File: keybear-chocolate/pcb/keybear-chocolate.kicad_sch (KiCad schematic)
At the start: 89 parts, among them J1 MJ-4PP-9, J2 OLED, J3 LED, P1 i2c-pin, P2 i2c-pin, SW1 SW_PUSH, SW10 SW_PUSH, SW11 SW_PUSH, SW12 SW_PUSH, SW13 SW_PUSH, SW14 SW_PUSH, SW15 SW_PUSH, SW16 SW_PUSH, SW17 SW_PUSH, SW18 SW_PUSH, SW19 SW_PUSH, SW2 SW_PUSH, SW20 SW_PUSH, SW21 SW_PUSH, SW25 Rotary_Encoder_Switch, SW3 SW_PUSH, SW4 SW_PUSH, SW5 SW_PUSH, SW6 SW_PUSH, SW7 SW_PUSH, SW8 SW_PUSH, SW9 SW_PUSH, U1 ProMicro

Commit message: updating keys
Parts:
- added D19, D23: D, kbd:D3_TH_SMD, symbol Device:D
- added L23: SK6812MINI, kbd:SK6812MINI_rev, symbol corne-chocolate-rescue:SK6812MINI-kbd
- added SW19, SW23: SW_PUSH, kbd:MX_ALPS_PG1350_noLed, symbol corne-chocolate-rescue:SW_PUSH-kbd
- L24: renamed from L23; footprint kbd:SK6812MINI_underglow -> kbd:SK6812MINI_rev
- L25: renamed from L24; footprint kbd:SK6812MINI_underglow -> kbd:SK6812MINI_rev
- L26: renamed from L25; footprint kbd:SK6812MINI_underglow -> kbd:SK6812MINI_rev
- L27: renamed from L26; footprint kbd:SK6812MINI_underglow -> kbd:SK6812MINI_rev
- L28: renamed from L27; footprint kbd:SK6812MINI_underglow -> kbd:SK6812MINI_rev
- L29: renamed from L28; footprint kbd:SK6812MINI_underglow -> kbd:SK6812MINI_rev
- SW1, SW2, SW3, SW4, SW5, SW6, SW7, SW8, SW9: footprint kbd:MX_ALPS_PG1350_noLed -> SofleChoc:Choc_Hotswap_SK6812MiniE
- renumbered D19 to D20, D20 to D21, D21 to D22, SW19 to SW20, SW20 to SW21, SW21 to SW22
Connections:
- net ENCA: now also U1.14 (B2)
- net ENCB: now also U1.13 (B6)
- net GND: now also L23.2 (VSS)
- net VCC: now also L23.4 (VDD)
- net col2: now also SW19.1
- net col3: now also SW23.1
- net row0: now also U1.8 (C6), D23.1 (K); no longer D1.1 (K), D2.1 (K), D3.1 (K), D4.1 (K), D5.1 (K), D6.1 (K), U1.7 (D4)
- net row1: now also D1.1 (K), D2.1 (K), D3.1 (K), D4.1 (K), D5.1 (K), D6.1 (K), U1.9 (D7); no longer D10.1 (K), D11.1 (K), D12.1 (K), D7.1 (K), D8.1 (K), D9.1 (K), U1.8 (C6)
- net row2: now also D10.1 (K), D11.1 (K), D12.1 (K), D7.1 (K), D8.1 (K), D9.1 (K), U1.10 (E6); no longer D13.1 (K), D14.1 (K), D15.1 (K), D16.1 (K), D17.1 (K), D18.1 (K), U1.9 (D7)
- net row3: now also D13.1 (K), D14.1 (K), D15.1 (K), D16.1 (K), D17.1 (K), D18.1 (K), U1.11 (B4); no longer D20.1 (K), D21.1 (K), D22.1 (K), U1.10 (E6)
- net row4: now reaches U1.12 (B5)
- net row4: now also D20.1 (K), D21.1 (K), D22.1 (K), D19.1 (K)
- net at L3.3 (DIN): now also L23.1 (DOUT); no longer L4.1 (DOUT)
- new net: L23.3 (DIN), L4.1 (DOUT)
- new net: D23.2 (A), SW23.2
- new net: D19.2 (A), SW19.2
- new net CS: U1.7 (D4)
- no-connect marks 6 -> 2
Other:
- moved on the sheet: D1, D10, D11, D12, D13, D14, D15, D16, D17, D18, D2, D20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

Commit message: updated latest kicad files
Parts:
- removed L23: SK6812MINI, kbd:SK6812MINI_rev, symbol corne-chocolate-rescue:SK6812MINI-kbd
- removed SW23: SW_PUSH, kbd:MX_ALPS_PG1350_noLed, symbol corne-chocolate-rescue:SW_PUSH-kbd
- added L19: SK6812MINI, kbd:SK6812MINI_rev, symbol corne-chocolate-rescue:SK6812MINI-kbd
- added SW19: SW_PUSH, kbd:Choc_Hotswap, symbol corne-chocolate-rescue:SW_PUSH-kbd
- D1, D10, D11, D12, D13, D14, D15, D16, D17, D18, D19, D20, D21, D22, D23, D3, D4, D5, D6, D7, D8, D9: footprint kbd:D3_TH_SMD -> kbd:D3_SMD
- D2: footprint kbd:D3_TH_SMD -> kbd:D3_SMD_v2
- SW10, SW11, SW12, SW13, SW14, SW15, SW16, SW17, SW18: footprint kbd:MX_ALPS_PG1350_noLed -> kbd:Choc_Hotswap
- SW20: renamed from SW19; footprint kbd:MX_ALPS_PG1350_noLed -> kbd:Choc_Hotswap
- SW21: renamed from SW20; footprint kbd:MX_ALPS_PG1350_noLed -> kbd:Choc_Hotswap
- SW22: renamed from SW21; footprint kbd:MX_ALPS_PG1350_noLed -> kbd:Choc_Hotswap
- SW23: renamed from SW22; footprint kbd:MX_ALPS_PG1350_noLed_1.75u -> kbd:Choc_Hotswap
- SW7, SW8, SW9: footprint SofleChoc:Choc_Hotswap_SK6812MiniE -> kbd:Choc_Hotswap
- renumbered L19 to L20, L20 to L21, L21 to L22, L22 to L23
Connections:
- net GND: now also L19.2 (VSS)
- net VCC: now also L19.4 (VDD)
- net col1: now also SW19.1
- net row0: now also D1.1 (K), D2.1 (K), D3.1 (K), D4.1 (K), D5.1 (K), D6.1 (K); no longer D23.1 (K)
- net row1: now also D10.1 (K), D11.1 (K), D12.1 (K), D7.1 (K), D8.1 (K), D9.1 (K); no longer D1.1 (K), D2.1 (K), D3.1 (K), D4.1 (K), D5.1 (K), D6.1 (K)
- net row2: now also D13.1 (K), D14.1 (K), D15.1 (K), D16.1 (K), D17.1 (K), D18.1 (K); no longer D10.1 (K), D11.1 (K), D12.1 (K), D7.1 (K), D8.1 (K), D9.1 (K)
- net row3: now also D19.1 (K), D20.1 (K), D21.1 (K), D22.1 (K), D23.1 (K); no longer D13.1 (K), D14.1 (K), D15.1 (K), D16.1 (K), D17.1 (K), D18.1 (K)
- net at L3.3 (DIN): now also L4.1 (DOUT)
- net at L14.3 (DIN): now also L19.1 (DOUT); no longer L20.1 (DOUT)
- net at D23.2 (A): now also SW19.2
- removed net row4: D19.1 (K), D20.1 (K), D21.1 (K), D22.1 (K), U1.12 (B5)
- new net: L19.3 (DIN), L20.1 (DOUT)
- no-connect marks 2 -> 3
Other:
- moved on the sheet: L24, L25, L26, L27, L28, L29, SW25, U1

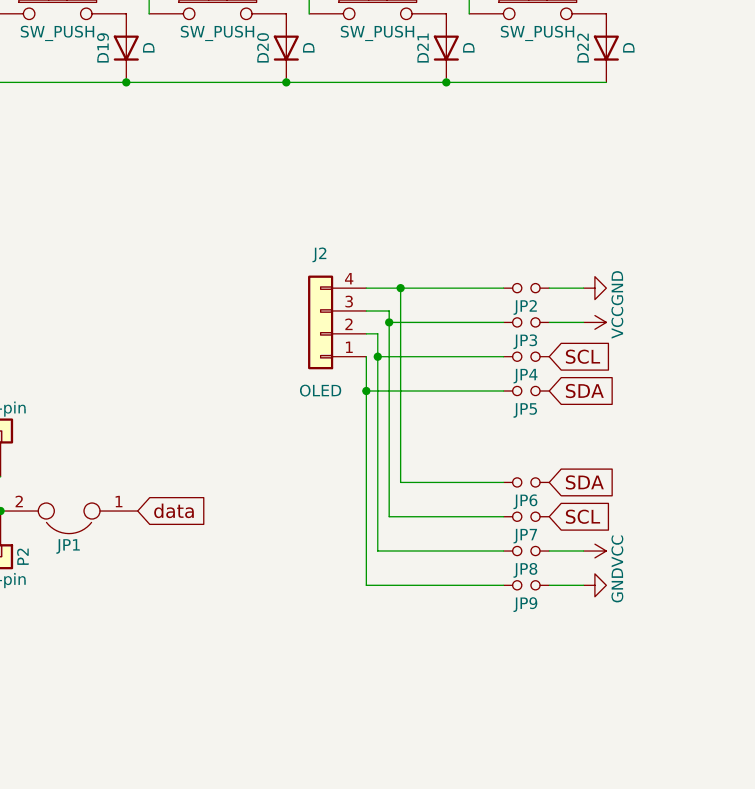
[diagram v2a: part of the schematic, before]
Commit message: OLED port updated to 5 pins
OLED port updated to 5 pins to support NiceView! out of the box
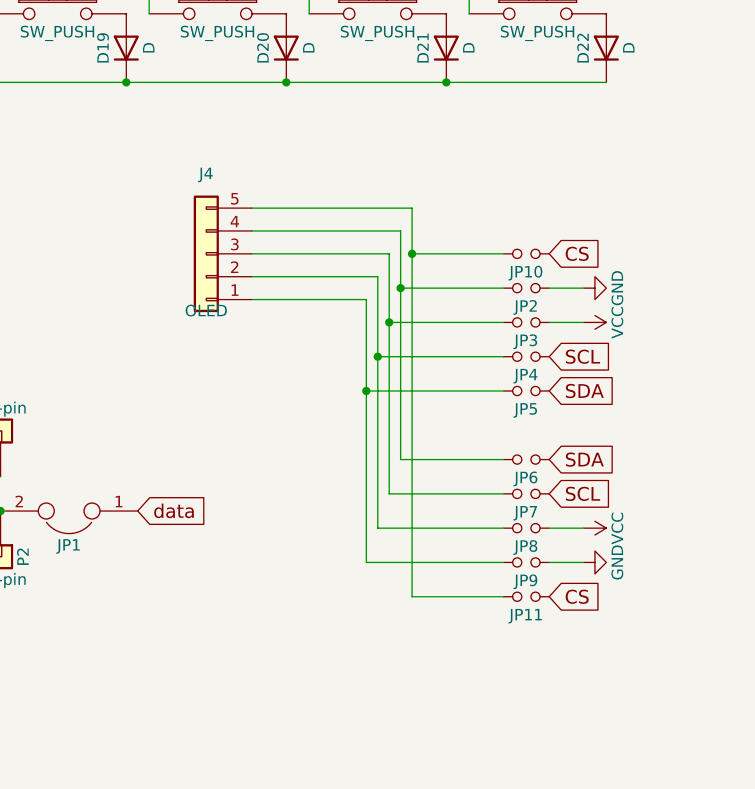
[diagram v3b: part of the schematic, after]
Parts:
- removed J2: OLED, kbd:OLED, symbol Connector_Generic:Conn_01x04
- added J4: OLED, kbd:OLED, symbol Connector_Generic:Conn_01x05
- added JP10, JP11: (no value), kbd:Jumper, symbol corne-chocolate-rescue:Jumper_NO_Small-Device
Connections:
- net CS: now also JP10.1, JP11.1
- net at JP5.2, JP9.2: now also J4.1 (Pin_1)
- net at JP4.2, JP8.2: now also J4.2 (Pin_2)
- net at JP3.2, JP7.2: now also J4.3 (Pin_3)
- net at JP2.2, JP6.2: now also J4.4 (Pin_4)
- new net: J4.5 (Pin_5), JP10.2, JP11.2
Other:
- moved on the sheet: JP6, JP7, JP8, JP9

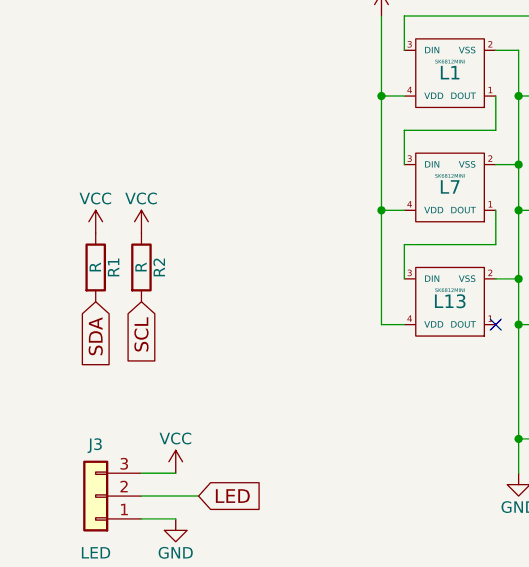
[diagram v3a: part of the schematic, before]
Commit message: OLED Resistence removed
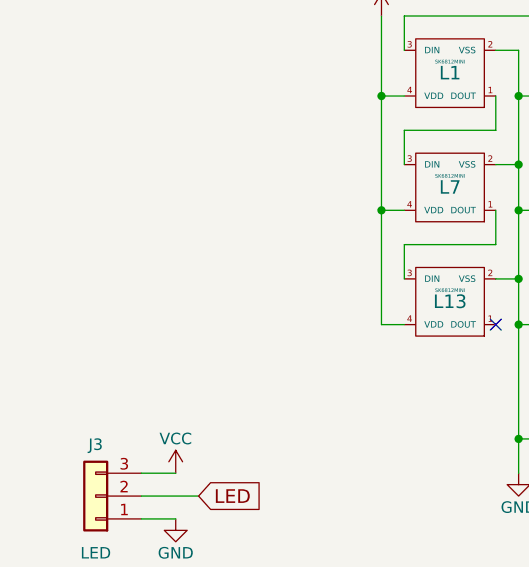
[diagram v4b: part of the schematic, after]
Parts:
- removed R1, R2: R, kbd:R, symbol Device:R
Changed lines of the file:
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@@
-    )
-  )
-  (global_label "SCL" (shape input) (at 30.48 163.83 270) (fields_autoplaced)
-    (effects (font (size 1.524 1.524)) (justify right))
-    (property "Intersheetrefs" "${INTERSHEET_REFS}" (at 30.48 170.8359 90)
-      (effects (font (size 1.27 1.27)) (justify right) hide)
     )
   )
@@
     (effects (font (size 1.1938 1.1938)) (justify right))
     (property "Intersheetrefs" "${INTERSHEET_REFS}" (at 23.7788 24.13 0)
-      (effects (font (size 1.27 1.27)) (justify right) hide)
-    )
-  )
-  (global_label "SDA" (shape input) (at 25.4 163.83 270) (fields_autoplaced)
-    (effects (font (size 1.524 1.524)) (justify right))
-    (property "Intersheetrefs" "${INTERSHEET_REFS}" (at 25.4 170.9085 90)
       (effects (font (size 1.27 1.27)) (justify right) hide)
     )
@@
         )
       )
-    )
-  )
-  (symbol (lib_id "Device:R") (at 25.4 160.02 0) (unit 1)
-    (in_bom yes) (on_board yes) (dnp no)
-    (property "Reference" "R1" (at 27.432 160.02 90)
-      (effects (font (size 1.27 1.27)))
-    )
-    (property "Value" "R" (at 25.4 160.02 90)
-      (effects (font (size 1.27 1.27)))
-    )
-    (property "Footprint" "kbd:R" (at 23.622 160.02 90)
-      (effects (font (size 1.27 1.27)) hide)
-    )
-    (property "Datasheet" "" (at 25.4 160.02 0)
-      (effects (font (size 1.27 1.27)) hide)
-    )
-    (pin "1")
-    (pin "2")
-    (instances
-      (project "keybear-chocolate"
-        (path "/b2404ab0-025a-473e-9fbb-0abc932972cf"
-          (reference "R1") (unit 1)
-        )
-      )
-    )
-  )
-  (symbol (lib_id "Device:R") (at 30.48 160.02 0) (unit 1)
-    (in_bom yes) (on_board yes) (dnp no)
-    (property "Reference" "R2" (at 32.512 160.02 90)
-      (effects (font (size 1.27 1.27)))
-    )
-    (property "Value" "R" (at 30.48 160.02 90)
-      (effects (font (size 1.27 1.27)))
-    )
-    (property "Footprint" "kbd:R" (at 28.702 160.02 90)
-      (effects (font (size 1.27 1.27)) hide)
-    )
-    (property "Datasheet" "" (at 30.48 160.02 0)
-      (effects (font (size 1.27 1.27)) hide)
-    )
-    (pin "1")
-    (pin "2")
-    (instances
-      (project "keybear-chocolate"
-        (path "/b2404ab0-025a-473e-9fbb-0abc932972cf"
-          (reference "R2") (unit 1)
-        )
-      )
-    )
-  )
-  (symbol (lib_id "power:VCC") (at 25.4 156.21 0) (unit 1)
-    (in_bom yes) (on_board yes) (dnp no)
-    (property "Reference" "#PWR021" (at 25.4 160.02 0)
-      (effects (font (size 1.27 1.27)) hide)
-    )
-    (property "Value" "VCC" (at 25.4 152.4 0)
-      (effects (font (size 1.27 1.27)))
-    )
-    (property "Footprint" "" (at 25.4 156.21 0)
-      (effects (font (size 1.27 1.27)) hide)
-    )
-    (property "Datasheet" "" (at 25.4 156.21 0)
-      (effects (font (size 1.27 1.27)) hide)
-    )
-    (pin "1")
-    (instances
-      (project "keybear-chocolate"
-        (path "/b2404ab0-025a-473e-9fbb-0abc932972cf"
-          (reference "#PWR021") (unit 1)
-        )
-      )
-    )
-  )
-  (symbol (lib_id "power:VCC") (at 30.48 156.21 0) (unit 1)
-    (in_bom yes) (on_board yes) (dnp no)
-    (property "Reference" "#PWR022" (at 30.48 160.02 0)
-      (effects (font (size 1.27 1.27)) hide)
-    )
-    (property "Value" "VCC" (at 30.48 152.4 0)
-      (effects (font (size 1.27 1.27)))
-    )
-    (property "Footprint" "" (at 30.48 156.21 0)
-      (effects (font (size 1.27 1.27)) hide)
-    )
-    (property "Datasheet" "" (at 30.48 156.21 0)
-      (effects (font (size 1.27 1.27)) hide)
-    )
-    (pin "1")
-    (instances
-      (project "keybear-chocolate"
-        (path "/b2404ab0-025a-473e-9fbb-0abc932972cf"
-          (reference "#PWR022") (unit 1)
-        )
-      )
